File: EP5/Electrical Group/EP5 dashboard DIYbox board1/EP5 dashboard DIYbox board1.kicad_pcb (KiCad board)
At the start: 2 copper layers, 138.2 x 72.5 mm, 136 parts, among them J1 pedal2-2, J10 12864, J11 pedal1-1, J12 pedal1-2, J13 5V and RTD, J2 pedal2-1, J3 MCU, J4 R1, J5 L1, J6 L2, J7 L3, J8 L4, J9 RTD, U1 Seg1, U10 74HC595, U11 74HC595, U12 74HC595, U13 74HC595, U14 74HC595, U15 74HC595, U16 74HC595, U17 74HC595, U2 Seg2, U5 Seg3, U6 Seg4, U7 74HC595, U8 74HC595, U9 74HC595

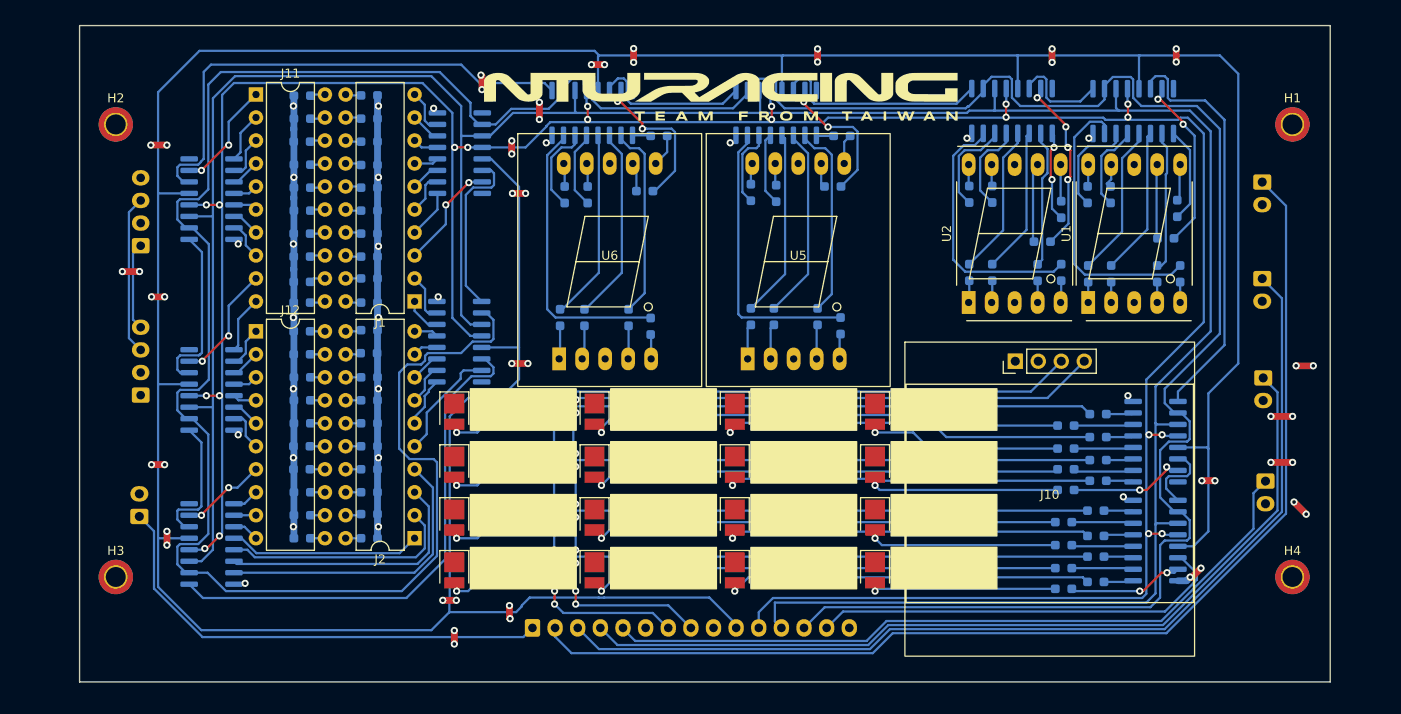
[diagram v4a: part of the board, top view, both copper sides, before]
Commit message: update dashboard board 1 & 2 to V2.0 to cancel isolation and use IDC socket
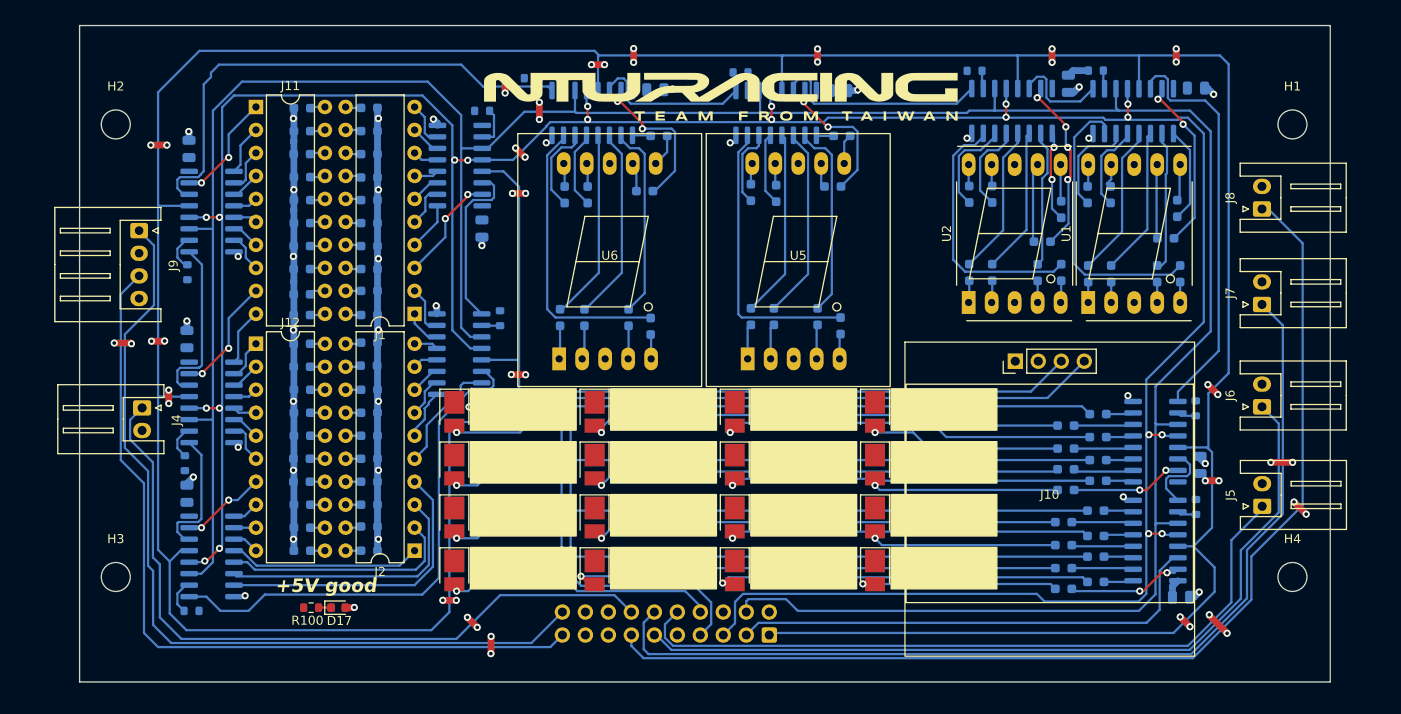
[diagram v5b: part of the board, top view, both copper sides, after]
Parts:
- removed J13: 5V and RTD, Connector_JST:JST_XH_S4B-XH-A_1x04_P2.50mm_Horizontal
- removed J3: MCU, Connector_JST:JST_XH_S15B-XH-A_1x15_P2.50mm_Horizontal
- added C1: 0u1 16V, Capacitor_SMD:C_0805_2012Metric, B.Cu at (79.7, 58.3)
- added C10: 0u1 16V, Capacitor_SMD:C_0805_2012Metric, B.Cu at (189.3, 107.9)
- added C11: 0u1 16V, Capacitor_SMD:C_0805_2012Metric, B.Cu at (191.4, 93.2)
- added C2: 0u1 16V, Capacitor_SMD:C_0805_2012Metric, B.Cu at (79.4, 79.3)
- added C3: 0u1 16V, Capacitor_SMD:C_0805_2012Metric, B.Cu at (79.4, 96.4)
- added C4: 0u1 16V, Capacitor_SMD:C_0805_2012Metric, B.Cu at (112.5, 86.9)
- added C5: 0u1 16V, Capacitor_SMD:C_0805_2012Metric, B.Cu at (112.0, 67.1)
- added C6: 0u1 16V, Capacitor_SMD:C_0805_2012Metric, B.Cu at (190.9, 51.6)
- added C7: 0u1 16V, Capacitor_SMD:C_0805_2012Metric, B.Cu at (176.8, 51.1)
- added C8: 0u1 16V, Capacitor_SMD:C_0805_2012Metric, B.Cu at (151.5, 51.9)
- added C9: 0u1 16V, Capacitor_SMD:C_0805_2012Metric, B.Cu at (131.2, 51.8)
- added D17: 5VGood, LED_SMD:LED_0603_1608Metric, F.Cu at (96.1, 109.0)
- added J14: screen, Connector_IDC:IDC-Header_2x10_P2.54mm_Vertical, B.Cu at (143.8, 112.0)
- added R100: 220R, Resistor_SMD:R_0603_1608Metric, F.Cu at (93.1, 109.0)
- added R69: 1k, Resistor_SMD:R_0603_1608Metric, B.Cu at (190.9, 97.9)
- added R70: 1k, Resistor_SMD:R_0603_1608Metric, B.Cu at (190.9, 87.0)
- added R71: 1k, Resistor_SMD:R_0603_1608Metric, B.Cu at (117.5, 50.5)
- added R72: 1k, Resistor_SMD:R_0603_1608Metric, B.Cu at (140.6, 49.9)
- added R73: 1k, Resistor_SMD:R_0603_1608Metric, B.Cu at (179.8, 49.7)
- added R74: 1k, Resistor_SMD:R_0603_1608Metric, B.Cu at (166.4, 49.7)
- added R75: 1k, Resistor_SMD:R_0603_1608Metric, B.Cu at (112.0, 54.1)
- added R76: 1k, Resistor_SMD:R_0603_1608Metric, B.Cu at (114.0, 77.0)
- added R97: 1k, Resistor_SMD:R_0603_1608Metric, B.Cu at (79.9, 109.4)
- added R98: 1k, Resistor_SMD:R_0603_1608Metric, B.Cu at (79.2, 93.1)
- added R99: 1k, Resistor_SMD:R_0603_1608Metric, B.Cu at (79.5, 72.0)
- D1, D10, D11, D12, D13, D14, D15, D16, D2, D3, D4, D5, D6, D7, D8, D9: footprint LED_SMD:LED_PLCC_2835 -> LED_SMD:LED_PLCC_2835_Handsoldering
- H1, H2, H3, H4: footprint MountingHole:MountingHole_2.2mm_M2_DIN965_Pad_TopBottom -> MountingHole:MountingHole_3.2mm_M3
- J4, J5, J6, J7, J8, J9: moved to F.Cu
- moved J4 12.0 mm to (74.5, 86.9), turned to -90 degrees
- moved J6 3.19 mm to (198.2, 86.8), turned to 90 degrees
- moved J8 2.98 mm to (198.2, 65.0), turned to 90 degrees
- moved J7 2.86 mm to (198.2, 75.5), turned to 90 degrees
- moved J5 2.80 mm to (198.2, 97.8), turned to 90 degrees
- moved J9 1.68 mm to (74.1, 67.4), turned to -90 degrees
- moved J1 1.38 mm to (104.6, 76.6)
- moved R50 1.38 mm to (99.6, 79.7)
- moved R54 1.38 mm to (99.6, 95.1)
- moved R57 1.38 mm to (99.6, 87.5)
- moved R61 1.38 mm to (99.6, 71.6)
- moved R63 1.38 mm to (99.6, 66.5)
- moved R82 1.38 mm to (92.2, 66.5)
- moved R84 1.38 mm to (92.1, 71.6)
- moved R88 1.38 mm to (92.1, 82.4)
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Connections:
- U10 pad 10: SRCLR -> Net-(U10-~{SRCLR})
- U11 pad 10: SRCLR -> Net-(U11-~{SRCLR})
- U12 pad 10: SRCLR -> Net-(U12-~{SRCLR})
- U13 pad 10: SRCLR -> Net-(U13-~{SRCLR})
- U14 pad 10: SRCLR -> Net-(U14-~{SRCLR})
- U15 pad 10: SRCLR -> Net-(U15-~{SRCLR})
- U16 pad 10: SRCLR -> Net-(U16-~{SRCLR})
- U17 pad 10: SRCLR -> Net-(U17-~{SRCLR})
- U7 pad 10: SRCLR -> Net-(U7-~{SRCLR})
- U8 pad 10: SRCLR -> Net-(U8-~{SRCLR})
- U9 pad 10: SRCLR -> Net-(U9-~{SRCLR})
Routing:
- net SRCLR: track 374.6 -> 0.00 mm
- net ButtonRTDlight: track 9.71 -> 94.3 mm
- net ButtonRTD_raw: track 17.6 -> 88.8 mm
- net ButtonL1_raw: track 53.1 -> 80.9 mm
- net OE: track 392.6 -> 416.0 mm
- net GND: track 98.8 -> 113.0 mm, vias 25 -> 36
- net SER: track 47.2 -> 53.7 mm
- net RCLK: track 316.9 -> 322.8 mm
- net ButtonR4_raw: track 126.6 -> 120.7 mm
- net ButtonR2_raw: track 97.1 -> 91.5 mm
- net +5V: track 41.3 -> 46.1 mm, vias 48 -> 47
- net Net-(U17-~{SRCLR}): track 0.00 -> 4.35 mm
- net SDA: track 94.5 -> 98.8 mm, vias 10 -> 8
- net Net-(U13-~{SRCLR}): track 0.00 -> 4.10 mm
- net Net-(U15-~{SRCLR}): track 0.00 -> 3.91 mm
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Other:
- board text added: "+5V good"
- board text added: "EP5 V2.0 dashboard 1 Jack Kuo"
- board text added: "GND"
- board text added: "N"
- board text added: "P"
- board text added: "RTD LED GND RTD button GND"
- board text added: "buttonL1"
- board text added: "buttonR1"
- board text added: "buttonR2"
- board text added: "buttonR3"
- board text added: "buttonR4"

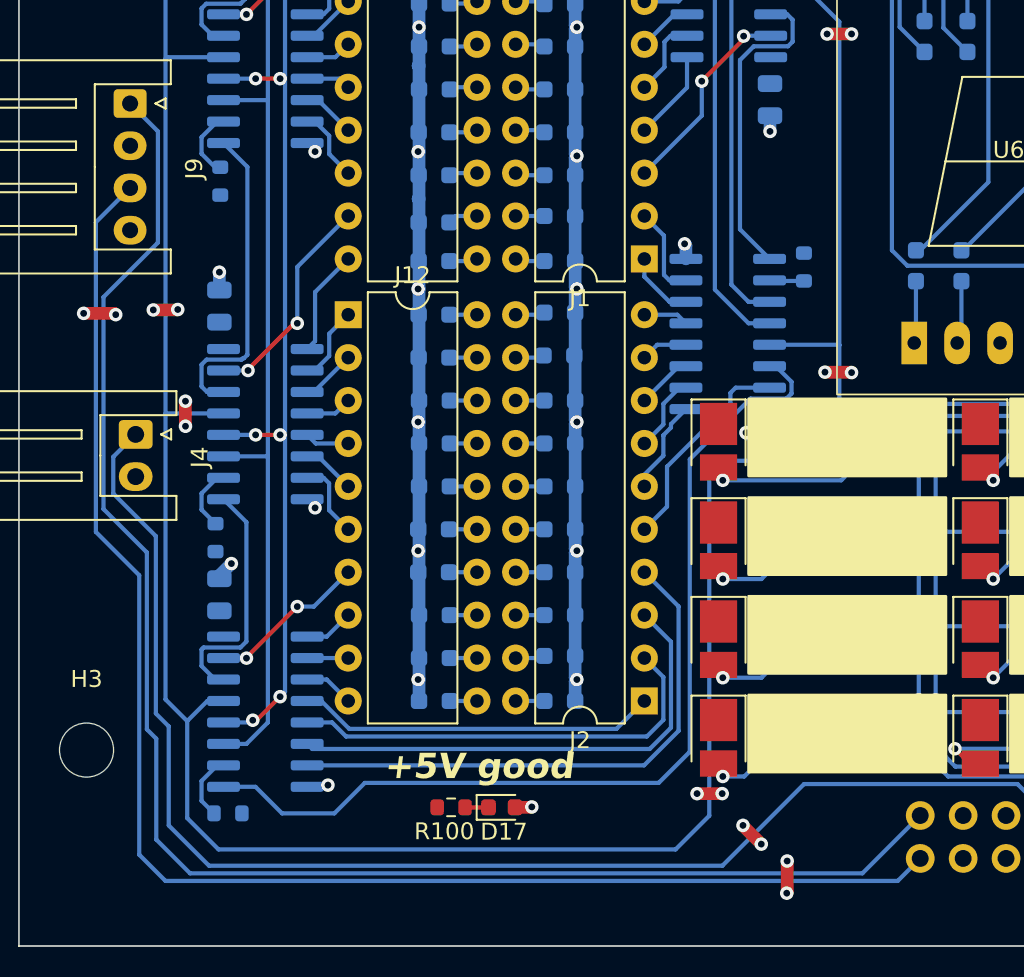
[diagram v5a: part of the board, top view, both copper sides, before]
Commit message: update dashboard board 1 to v2.1
fix RTD button light, GND should be 5V, and signal using open drain to control
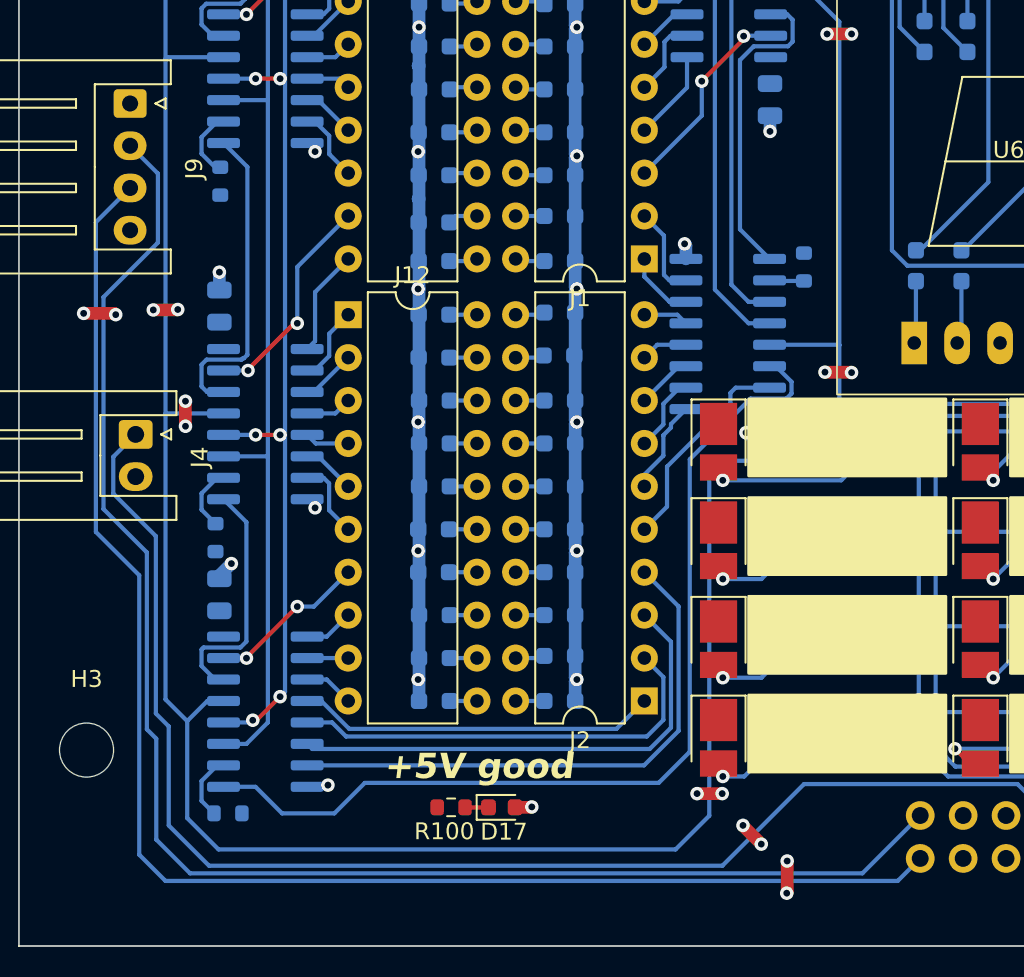
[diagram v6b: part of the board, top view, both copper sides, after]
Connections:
- J9 pad 1: ButtonRTDlight -> +5V
- J9 pad 2: GND -> ButtonRTDlight
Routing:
- net ButtonRTDlight: track 94.3 -> 91.8 mm
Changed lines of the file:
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@@
   (title_block
     (title "EP5 dashboard screen board")
-    (date "2024-06-27")
-    (rev "2.0")
+    (date "2024-07-20")
+    (rev "2.1")
     (company "NTURacing")
     (comment 1 "郭哲明")
@@
       (stroke (width 0.1) (type solid)) (layer "F.Fab"))
     (pad "1" thru_hole roundrect (at 0 0 270) (size 1.7 1.95) (drill 0.95) (layers "*.Cu" "*.Mask") (roundrect_rratio 0.1470588235)
-      (net 161 "ButtonRTDlight") (pinfunction "Pin_1") (pintype "passive"))
+      (net 142 "+5V") (pinfunction "Pin_1") (pintype "passive"))
     (pad "2" thru_hole oval (at 2.5 0 270) (size 1.7 1.95) (drill 0.95) (layers "*.Cu" "*.Mask")
-      (net 195 "GND") (pinfunction "Pin_2") (pintype "passive"))
+      (net 161 "ButtonRTDlight") (pinfunction "Pin_2") (pintype "passive"))
     (pad "3" thru_hole oval (at 5 0 270) (size 1.7 1.95) (drill 0.95) (layers "*.Cu" "*.Mask")
       (net 203 "ButtonRTD_raw") (pinfunction "Pin_3") (pintype "passive"))
@@
   (segment (start 189.2026 98.7166) (end 188.911 98.425) (width 0.25) (layer "B.Cu") (net 160))
   (segment (start 190.9064 98.7166) (end 189.2026 98.7166) (width 0.25) (layer "B.Cu") (net 160))
-  (segment (start 72.5678 91.3638) (end 75.1332 93.9292) (width 0.25) (layer "B.Cu") (net 161))
-  (segment (start 74.1426 67.3608) (end 75.7885 69.0067) (width 0.25) (layer "B.Cu") (net 161))
-  (segment (start 77.6914 112.9212) (end 117.4822 112.9212) (width 0.25) (layer "B.Cu") (net 161))
-  (segment (start 72.5678 78.8162) (end 72.5678 91.3638) (width 0.25) (layer "B.Cu") (net 161))
-  (segment (start 75.692 104.9528) (end 75.692 110.9218) (width 0.25) (layer "B.Cu") (net 161))
-  (segment (start 75.1332 104.394) (end 75.692 104.9528) (width 0.25) (layer "B.Cu") (net 161))
-  (segment (start 75.7885 69.0067) (end 75.7885 75.5955) (width 0.25) (layer "B.Cu") (net 161))
-  (segment (start 75.692 110.9218) (end 77.6914 112.9212) (width 0.25) (layer "B.Cu") (net 161))
-  (segment (start 75.7885 75.5955) (end 72.5678 78.8162) (width 0.25) (layer "B.Cu") (net 161))
-  (segment (start 117.4822 112.9212) (end 120.904 109.4994) (width 0.25) (layer "B.Cu") (net 161))
-  (segment (start 75.1332 93.9292) (end 75.1332 104.394) (width 0.25) (layer "B.Cu") (net 161))
+  (segment (start 75.1332 93.9292) (end 72.5678 91.3638) (width 0.25) (layer "B.Cu") (net 161))
+  (segment (start 75.7885 75.5955) (end 75.7885 71.5067) (width 0.25) (layer "B.Cu") (net 161))
+  (segment (start 75.7885 71.5067) (end 74.1426 69.8608) (width 0.25) (layer "B.Cu") (net 161))
+  (segment (start 72.5678 91.3638) (end 72.5678 78.8162) (width 0.25) (layer "B.Cu") (net 161))
+  (segment (start 72.5678 78.8162) (end 75.7885 75.5955) (width 0.25) (layer "B.Cu") (net 161))
+  (segment (start 75.692 104.9528) (end 75.1332 104.394) (width 0.25) (layer "B.Cu") (net 161))
+  (segment (start 117.4822 112.9212) (end 77.6914 112.9212) (width 0.25) (layer "B.Cu") (net 161))
+  (segment (start 75.1332 104.394) (end 75.1332 93.9292) (width 0.25) (layer "B.Cu") (net 161))
+  (segment (start 75.692 110.9218) (end 75.692 104.9528) (width 0.25) (layer "B.Cu") (net 161))
+  (segment (start 77.6914 112.9212) (end 75.692 110.9218) (width 0.25) (layer "B.Cu") (net 161))
+  (segment (start 120.904 109.4994) (end 117.4822 112.9212) (width 0.25) (layer "B.Cu") (net 161))
   (segment (start 138.6078 106.299) (end 138.6298 106.277) (width 0.25) (layer "F.Cu") (net 162))
   (segment (start 138.6298 106.277) (end 139.954 106.277) (width 0.25) (layer "F.Cu") (net 162))

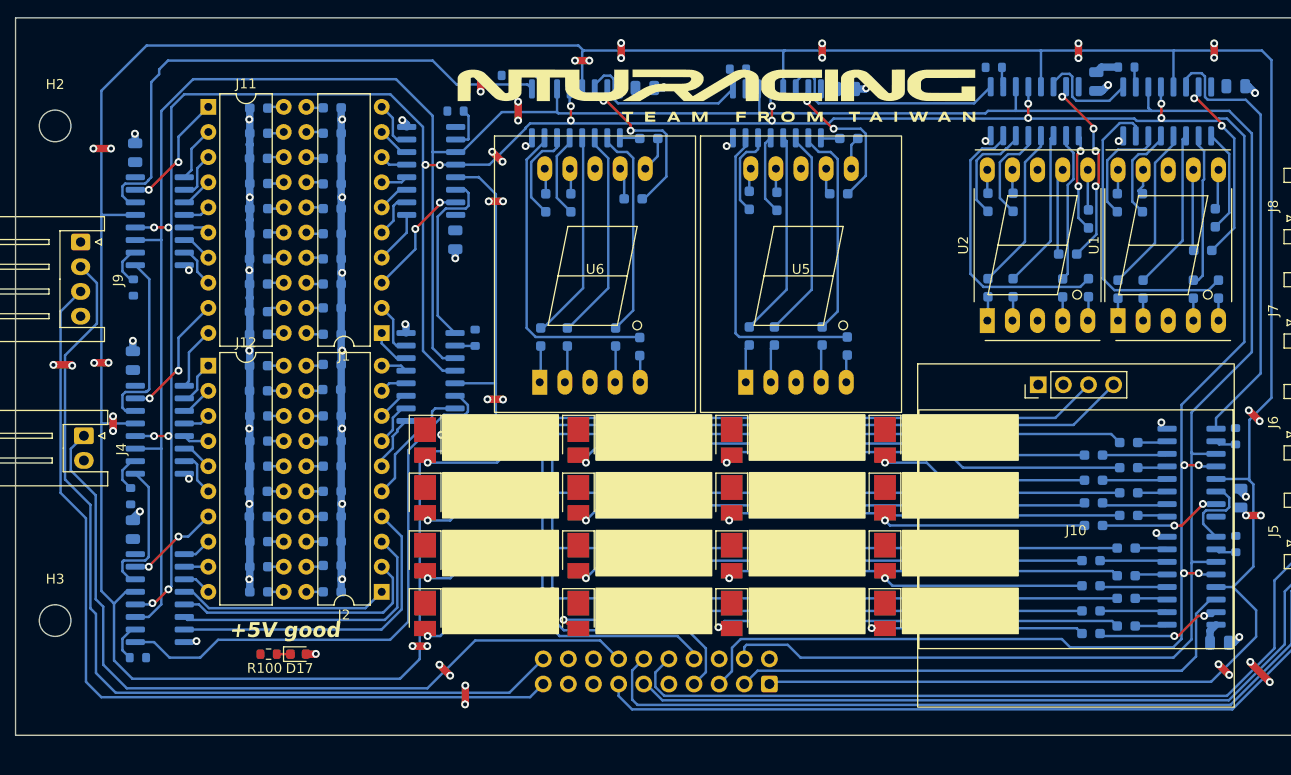
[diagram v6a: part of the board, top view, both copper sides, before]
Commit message: update dashboard board 2 (screen) to V2.2
fix I2C pinout to match OLED module
change RTD light to open drain version
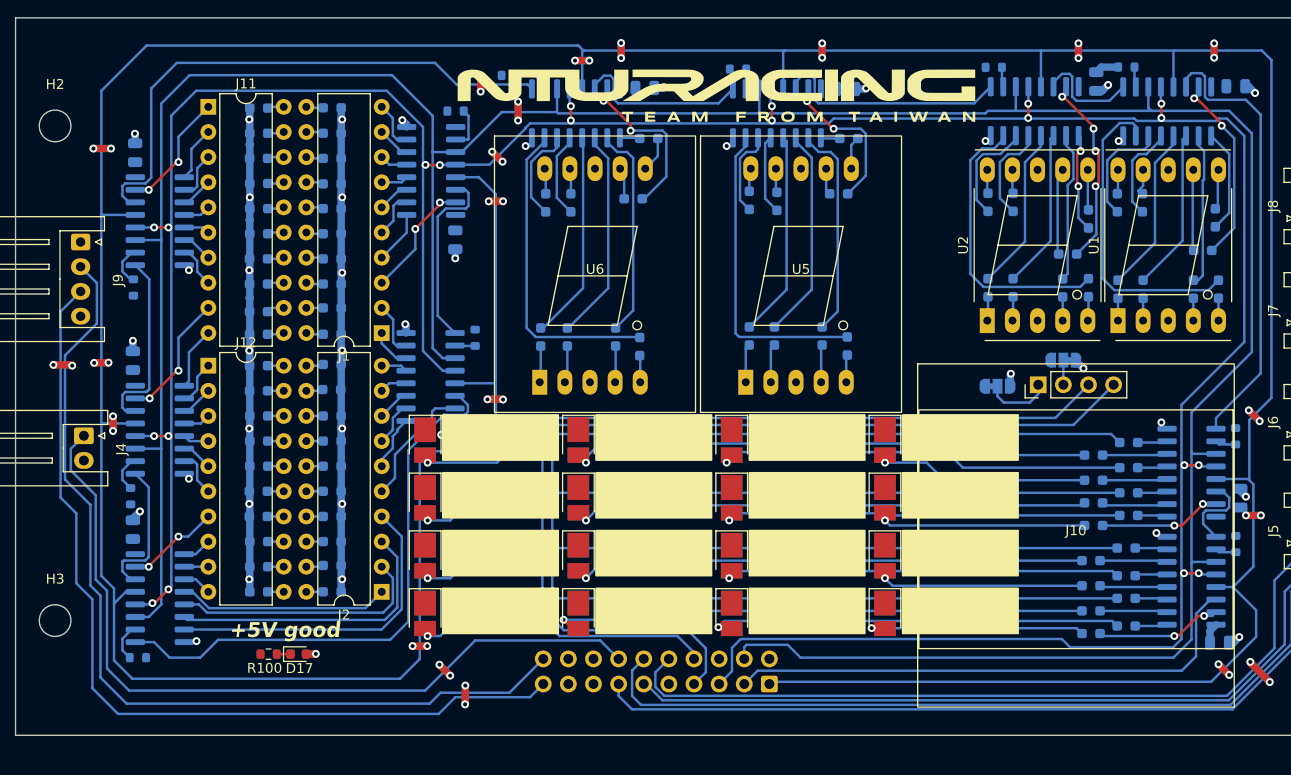
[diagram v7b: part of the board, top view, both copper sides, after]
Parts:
- added JP1: OLED_P1, Jumper:SolderJumper-3_P1.3mm_Bridged12_RoundedPad1.0x1.5mm, B.Cu at (166.8, 81.9)
- added JP2: OLED_P2, Jumper:SolderJumper-3_P1.3mm_Bridged12_RoundedPad1.0x1.5mm, B.Cu at (173.5, 79.3)
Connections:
- J10 pad 1: +5V -> Net-(J10-Pin_1)
- J10 pad 2: GND -> Net-(J10-Pin_2)
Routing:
- net Net-(J10-Pin_1): track 0.00 -> 6.69 mm
- net Net-(J10-Pin_2): track 0.00 -> 2.49 mm
- net GND: track 113.0 -> 115.4 mm, vias 36 -> 38
- net ButtonRTD_raw: track 88.8 -> 90.2 mm
- net ButtonRTDlight: track 91.8 -> 92.7 mm
- net Seg4End: track 56.3 -> 55.5 mm
- net SRCLK: track 316.7 -> 317.5 mm
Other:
- board text added: "5V"
- board text added: "5V RTD LED RTD button GND"
- board text added: "EP5 V2.2 dashboard 1 Jack Kuo"
- board text added: "SCL"
- board text added: "SDA"
- board text removed: "EP5 V2.0 dashboard 1 Jack Kuo"
- board text removed: "RTD LED GND RTD button GND"
